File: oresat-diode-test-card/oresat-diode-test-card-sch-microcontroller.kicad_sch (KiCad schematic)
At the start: 21 parts, among them J7 ORESAT-DEBUG-CONNECTOR-ALL, U1 TCAN330, U7 STM32F091C, X2 CRYSTAL-WITH-GND

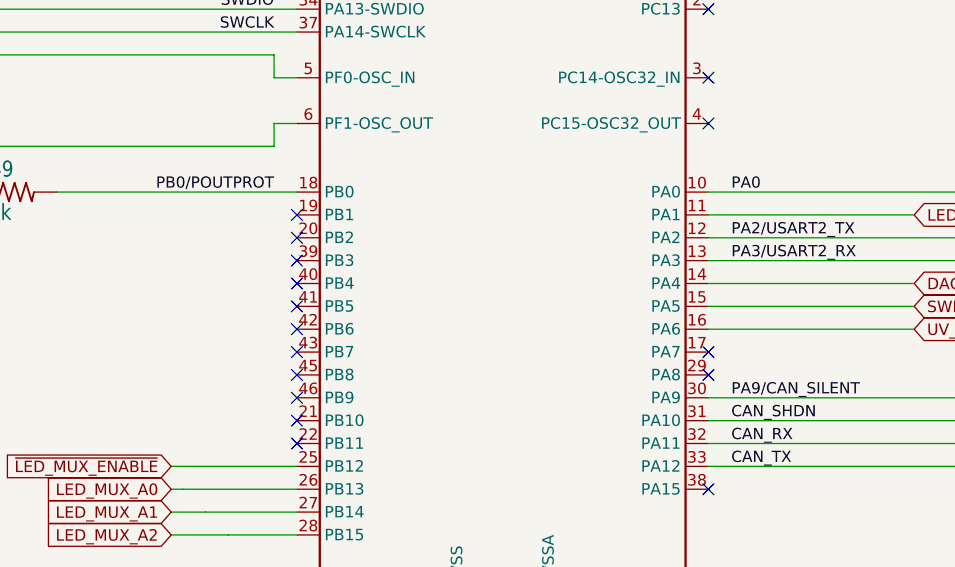
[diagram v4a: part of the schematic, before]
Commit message: added test points and trace width edits
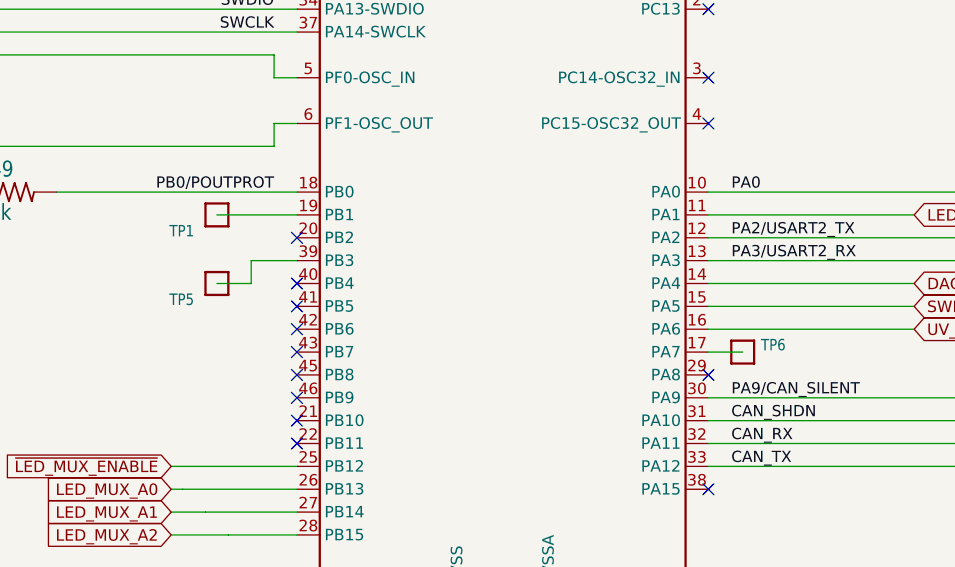
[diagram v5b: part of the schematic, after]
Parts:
- added TP1, TP5, TP6: TEST-POINT-LARGE-SQUARE, oresat-proto-card:1X01, symbol oresat-proto-card-eagle-import:TEST-POINT-LARGE-SQUARE
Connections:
- net at U7.17 (PA7): now also TP6.1
- net at U7.19 (PB1): now also TP1.1
- net at U7.39 (PB3): now also TP5.1
- no-connect marks 21 -> 18

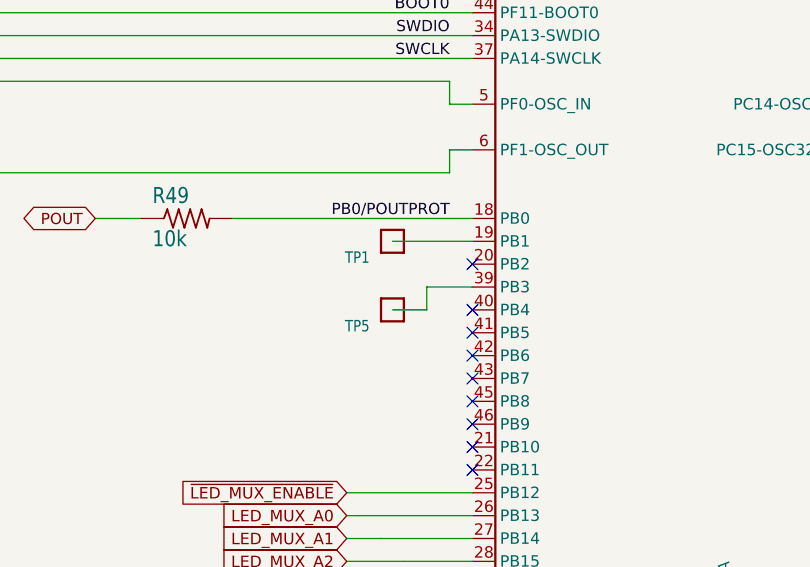
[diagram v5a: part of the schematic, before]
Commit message: Fix OPD weirdness, lots of little polishing including power plane movement and thicker traces.
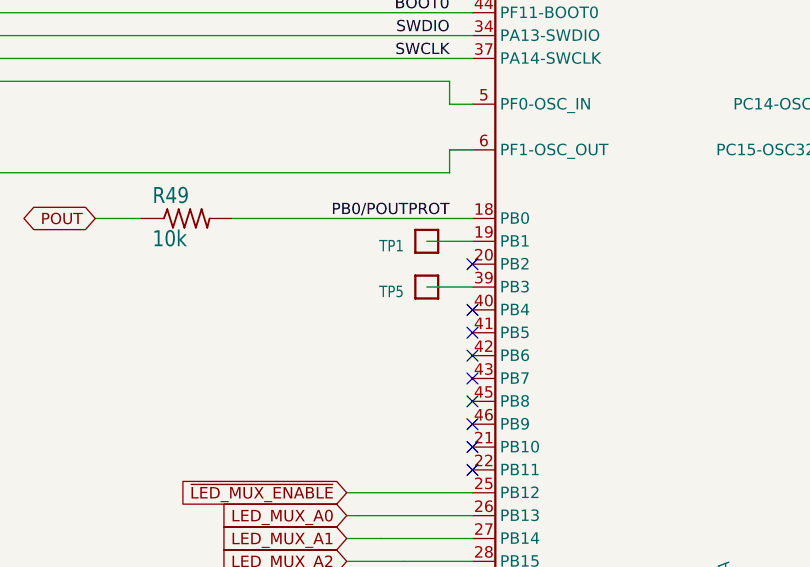
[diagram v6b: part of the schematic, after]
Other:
- moved on the sheet: TP1, TP5
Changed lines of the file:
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@@
 	(wire
 		(pts
-			(xy 186.69 100.33) (xy 182.88 100.33)
-		)
-		(stroke
-			(width 0)
-			(type default)
-		)
-	)
-	(wire
-		(pts
 			(xy 227.33 31.75) (xy 227.33 34.29)
 		)
@@
 	(wire
 		(pts
-			(xy 182.88 92.71) (xy 191.77 92.71)
+			(xy 186.69 92.71) (xy 191.77 92.71)
 		)
 		(stroke
@@
 	(wire
 		(pts
-			(xy 186.69 97.79) (xy 186.69 100.33)
-		)
-		(stroke
-			(width 0)
-			(type default)
-		)
-	)
-	(wire
-		(pts
 			(xy 189.23 74.93) (xy 189.23 77.47)
 		)
@@
 	(symbol
 		(lib_id "oresat-proto-card-eagle-import:TEST-POINT-LARGE-SQUARE")
-		(at 182.88 100.33 0)
+		(at 186.69 97.79 0)
 		(mirror y)
 		(unit 1)
@@
 		(dnp no)
 		(property "Reference" "TP5"
-			(at 180.34 102.87 0)
+			(at 184.15 99.06 0)
 			(effects
 				(font
@@
 		)
 		(property "Value" "TEST-POINT-LARGE-SQUARE"
-			(at 182.88 100.33 0)
+			(at 186.69 97.79 0)
 			(effects
 				(font
@@
 		)
 		(property "Footprint" "oresat-proto-card:1X01"
-			(at 182.88 100.33 0)
+			(at 186.69 97.79 0)
 			(effects
 				(font
@@
 		)
 		(property "Datasheet" ""
-			(at 182.88 100.33 0)
+			(at 186.69 97.79 0)
 			(effects
 				(font
@@
 		)
 		(property "Description" ""
-			(at 182.88 100.33 0)
+			(at 186.69 97.79 0)
 			(effects
 				(font
@@
 	(symbol
 		(lib_id "oresat-proto-card-eagle-import:TEST-POINT-LARGE-SQUARE")
-		(at 182.88 92.71 0)
+		(at 186.69 92.71 0)
 		(mirror y)
 		(unit 1)
@@
 		(dnp no)
 		(property "Reference" "TP1"
-			(at 180.34 95.25 0)
+			(at 184.15 93.98 0)
 			(effects
 				(font
@@
 		)
 		(property "Value" "TEST-POINT-LARGE-SQUARE"
-			(at 182.88 92.71 0)
+			(at 186.69 92.71 0)
 			(effects
 				(font
@@
 		)
 		(property "Footprint" "oresat-proto-card:1X01"
-			(at 182.88 92.71 0)
+			(at 186.69 92.71 0)
 			(effects
 				(font
@@
 		)
 		(property "Datasheet" ""
-			(at 182.88 92.71 0)
+			(at 186.69 92.71 0)
 			(effects
 				(font
@@
 		)
 		(property "Description" ""
-			(at 182.88 92.71 0)
+			(at 186.69 92.71 0)
 			(effects
 				(font

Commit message: Added BOM
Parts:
- C13, C14, C15, C18, C19, C20, C21, D5, R47, R48, R49, U1, X2: DST (none) -> Digi-Key
- U7: DPN 497-18516-ND -> 497-17364-ND; DST (none) -> Digi-Key; MPN STM32F042K6T7 -> STM32F091CCT7

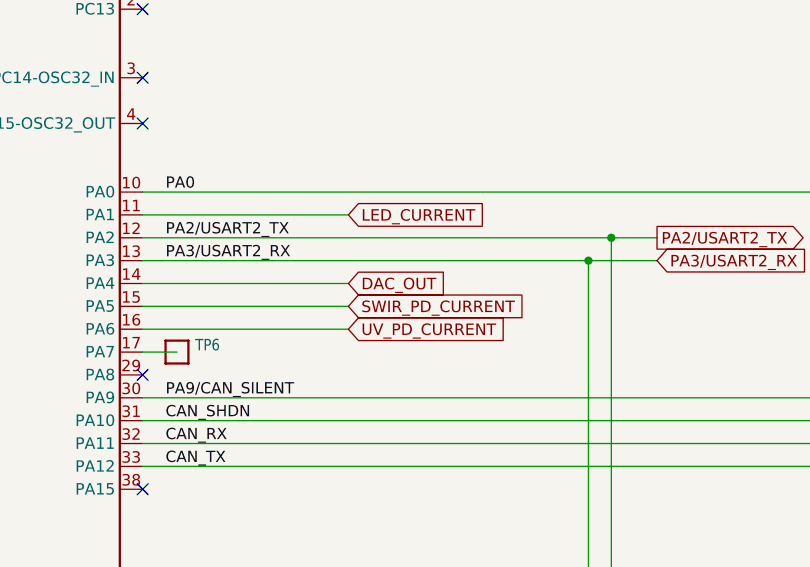
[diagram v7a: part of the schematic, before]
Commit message: BOM changes! Now up to date.
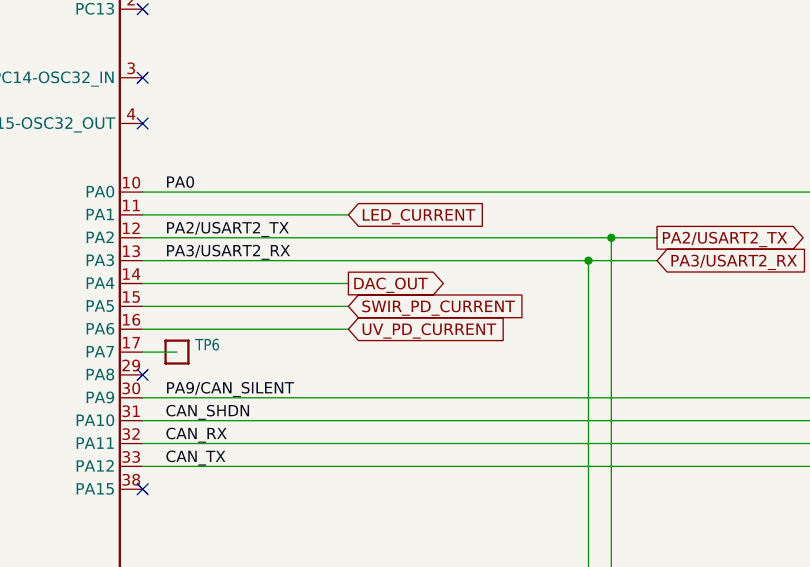
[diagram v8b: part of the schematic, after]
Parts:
- C13, C14, C19, C20, C21: DIS Digi-Key -> (none); DPN 1276-1001-1-ND -> 587-3472-1-ND; DST Digi-Key -> DigiKey; MFR Samsung -> Taiyo Yuden; MPN CL05B104KO5NNNC -> TMK107BJ104KAHT
- C15, C18: DIS Digi-Key -> (none); DPN 1276-6601-1-ND -> 490-11157-2-ND; DST Digi-Key -> DigiKey; MFR Samsung -> Murata Electronics; MPN CL05C200JB51PNC -> GCM1885C2A200JA16D
- D5: DIS Digi-Key -> (none); DPN 1830-1064-1-ND -> 732-150060AS75000CT-ND; DST Digi-Key -> DigiKey; MFR Inolux -> Wurth; MPN IN-S63AT5A -> 150060AS75000
- J7: DPN (none) -> A100287CT-ND; DST (none) -> DigiKey; MFR (none) -> TE; MPN (none) -> 2-1734592-0
- R47, R49: DIS Digi-Key -> (none); DPN 311-10.0KLRCT-ND -> RMCF0603FT10K0CT-ND; DST Digi-Key -> DigiKey; MFR Yageo -> Stackpole Electronics Inc; MPN RC0402FR-0710KL -> RMCF0603FT10K0
- R48: DIS Digi-Key -> (none); DPN A129632CT-ND -> RMCF0603FT2K70CT-ND; DST Digi-Key -> DigiKey; MFR TE Connectivity -> Stackpole Electronics Inc; MPN CRGCQ0402F2K7 -> RMCF0603FT2K70
- TP1, TP25, TP26, TP27, TP28, TP29, TP30, TP5, TP6: DPN (none) -> N/A; DST (none) -> N/A; MFR (none) -> N/A; MPN (none) -> N/A; now left out of the parts list
- U1, U7, X2: DIS Digi-Key -> (none); DST Digi-Key -> DigiKey
